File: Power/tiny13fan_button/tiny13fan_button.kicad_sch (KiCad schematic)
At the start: 22 parts, among them J1 CONN01PIN, J3 FAN, J4 12V, J6 5V, J8 ON/OFF out, SW1 SWITCH1, U2 ATtiny13V-10S

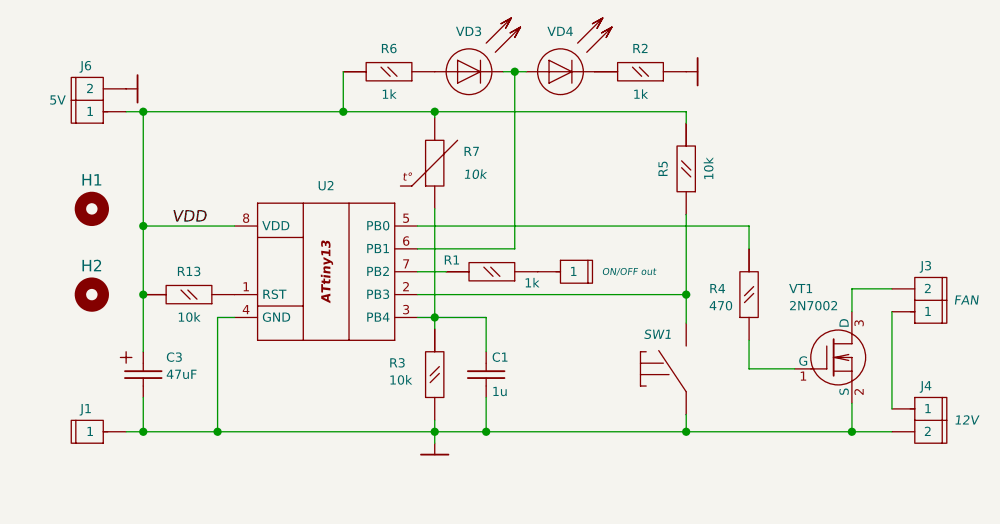
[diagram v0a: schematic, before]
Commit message: rename butoo fan
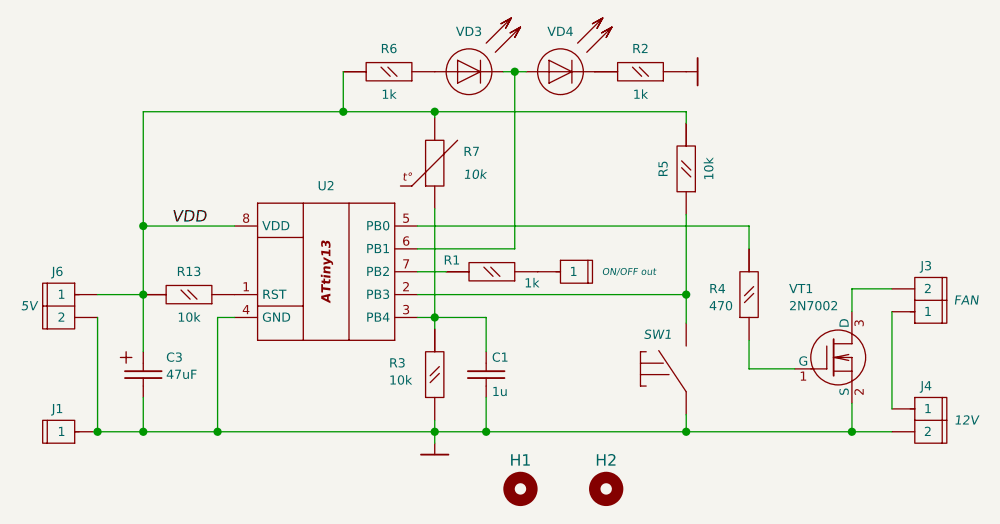
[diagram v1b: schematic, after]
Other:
- moved on the sheet: H1, H2, J1, J6
